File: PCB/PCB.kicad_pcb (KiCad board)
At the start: 2 copper layers, 418.3 x 124.6 mm, 417 parts, among them J2 Conn_OLED_I2C, U1 74AHCT125

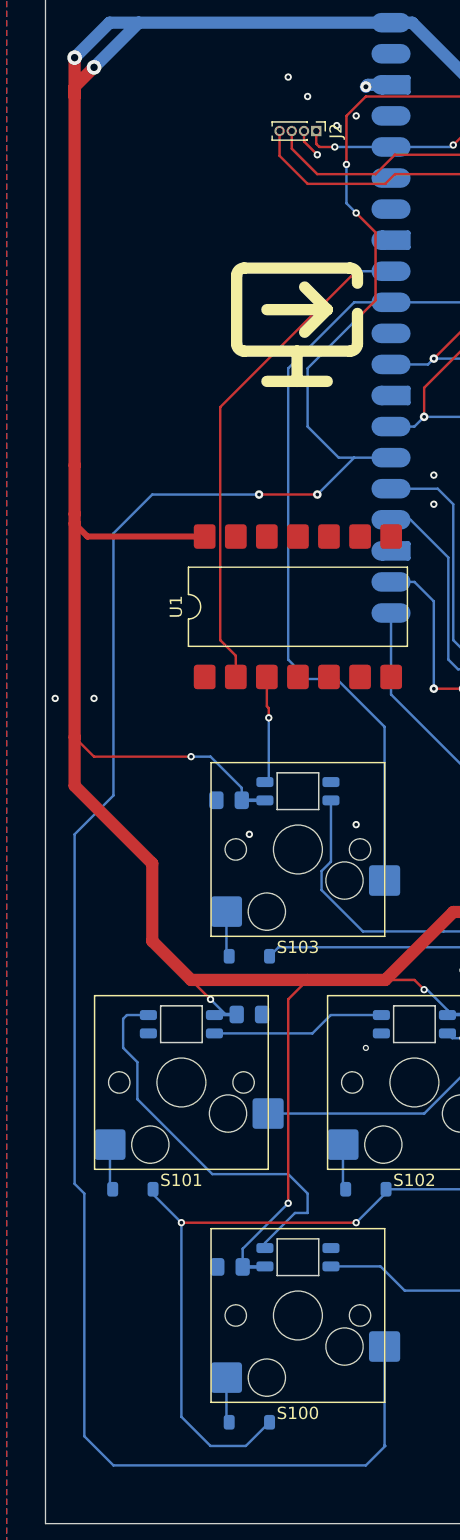
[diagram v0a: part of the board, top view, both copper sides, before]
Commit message: added decoupling capacitor near level shifter
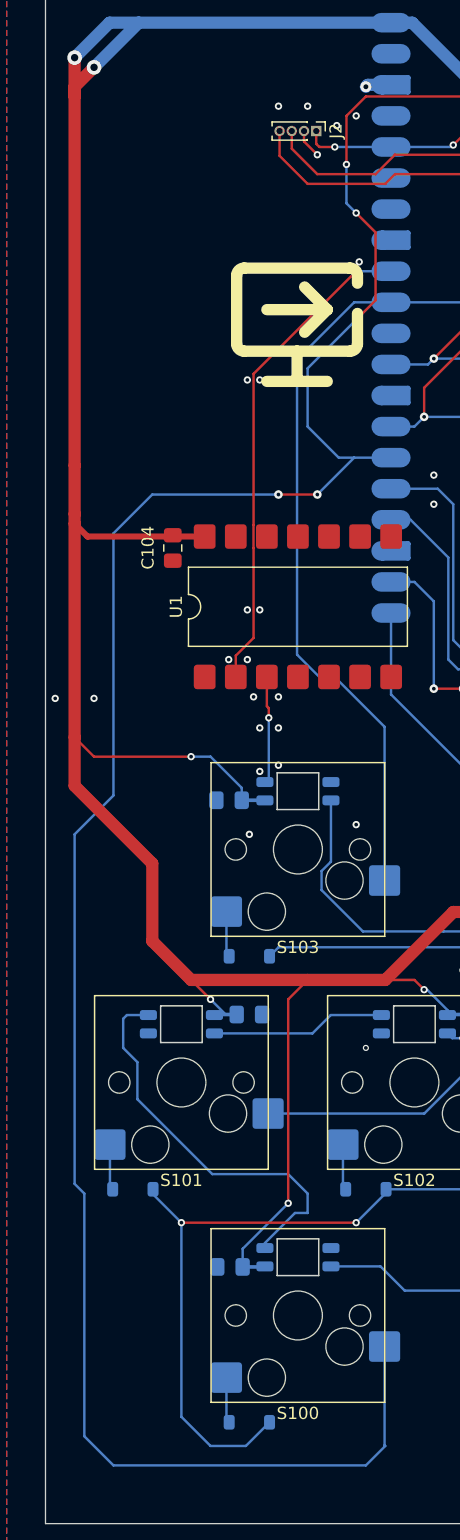
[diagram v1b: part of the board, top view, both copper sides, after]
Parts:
- added C104: 100nF, Capacitor_SMD:C_0805_2012Metric_Pad1.18x1.45mm_HandSolder, F.Cu at (76.5, 185.8)
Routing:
- net COL 13: track 415.8 -> 414.5 mm
- net LED GPIO: track 41.1 -> 40.1 mm
- net GND: vias 294 -> 306
- net (no net): vias 8 -> 10
